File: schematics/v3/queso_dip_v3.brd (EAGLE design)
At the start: 41 x 50 mm, 43 parts, among them U1 PRTR5V0U2X, U2 PRTR5V0U2X, U3 PRTR5V0U2X, U4 PRTR5V0U2X, U5 PRTR5V0U2X

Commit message: added new version
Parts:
- removed R2: ?, rcl:R0805
- removed U$4, U$6, U$7: USB_TYPE_A_FEMALE_TH, imcom:USB_TYPE_A_FEMALE_TH
- added Q1: FOXSDLF/120-20, adafruit:SM49
- added SJ2: (no value), SparkFun-Retired:SJ_2
- added X1, X2, X3, X4: USB-A-HU, con-usb:USB-A-HU
- C1, C2, C3, C4, C5, C6: value 10uF -> VJ1210V106ZXJTW1BC
- F1, F2, F3, F4: value (none) -> PTS12066V110
- LED1, LED2, LED3, LED4, LED5: value (none) -> 150080BS75000
- R5, R6, R7: value 330R -> ERJ-6ENF3300V
- U$10: value (none) -> USB-PWR; device adafruit:CERM_OSC -> adafruit:USB-MINIB-THM-MOLEX-PWRONLY
- U$3: value USB_TYPE_A_FEMALE_TH -> MP1584EN; device imcom:USB_TYPE_A_FEMALE_TH -> power_supply:MP1584EN
- U$8: value USB-MINIB-5PIN -> 10118194-0001LF
- U1, U2, U3, U4, U5: value PRTR5V0U2X -> PRTR5V0U2X,215
- moved PAD1 46.4 mm to (26.5, 46.8)
- moved PAD2 46.4 mm to (31.5, 46.8)
- moved U$3 26.6 mm to (22.9, 27.6), turned to 90 degrees
- moved U$9 24.6 mm to (9.70, 10.0), turned to 0 degrees
- moved U$10 22.6 mm to (12.1, 3.50), turned to 0 degrees
- moved U5 14.9 mm to (10.2, 25.0)
- moved C6 12.8 mm to (18.0, 30.3), turned to 270 degrees
- moved F4 6.70 mm to (27.2, 10.1), turned to 270 degrees
- moved C5 6.38 mm to (23.7, 29.4), turned to 180 degrees
- moved C1 5.02 mm to (21.1, 10.6), flipped to the top, turned to 0 degrees
- moved LED4 4.00 mm to (14.0, 36.5)
- moved LED5 4.00 mm to (11.5, 36.5)
- moved R6 3.86 mm to (16.3, 35.9)
- moved C3 3.13 mm to (24.2, 24.4)
- moved F1 3.06 mm to (27.4, 24.4), flipped to the bottom
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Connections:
- removed net N$23: R2.1, U$1.26
- removed net N$9: F2.2, U$7.1
- new net N$1: F2.2, X1.VBUS
- new net VOUT2: SJ2.2, U$3.VOUT
- new net V_UP: U$1.18, U$8.VBUS
- net CHR_IN: now also SJ2.1
- net DM1: now also X4.D-; no longer U$3.2
- net DM2: now also X3.D-; no longer U$4.2
- net DM3: now also X2.D-; no longer U$6.2
- net DM4: now also X1.D-; no longer U$7.2
- net DP1: now also X4.D+; no longer U$3.3
- net DP2: now also X3.D+; no longer U$4.3
- net DP3: now also X2.D+; no longer U$6.3
- net DP4: now also X1.D+; no longer U$7.3
- net GND: now also U$1.27, U$10.GND, U$3.GNDIN, U$3.GNDOUT, X1.GND, X2.GND, X3.GND, X4.GND; no longer U$10.P$2, U$3.4, U$4.4, U$6.4, U$7.4
- net N$10: now also X2.VBUS; no longer U$6.1
- net N$11: now also X3.VBUS; no longer U$4.1
- net N$12: now also X4.VBUS; no longer U$3.1
- net N$27: now also Q1.2; no longer U$10.P$1
- net N$28: now also Q1.1; no longer U$10.P$3
- net VCC: now also U$1.25, U$1.26, U$10.VBUS; no longer R2.2
- net VIN: now also U$3.VIN
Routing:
- net GND: track 398.2 -> 514.5 mm, vias 10 -> 7
- net VIN: track 36.3 -> 99.7 mm
- net V_UP: track 0.00 -> 22.1 mm, vias 0 -> 1
- net VOUT: track 8.87 -> 29.0 mm
- net VCC: track 152.2 -> 165.7 mm, vias 11 -> 9
- net N$18: track 39.7 -> 30.7 mm
- net DM2: track 32.7 -> 24.1 mm
- net N$23: track 8.09 -> 0.00 mm
- net N$32: track 23.7 -> 17.8 mm
- net N$28: track 8.02 -> 13.9 mm, vias 0 -> 1
- net DP4: track 23.5 -> 18.7 mm
- net DMU: track 31.4 -> 35.8 mm, vias 1 -> 2
- net DPU: track 31.4 -> 35.7 mm, vias 1 -> 2
- net N$9: track 3.38 -> 0.00 mm
- net DM3: track 23.6 -> 26.7 mm
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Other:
- board text added: "JKW v0.2"
- board text added: "QUESO DIP"
- board text removed: "SALSA DIP"

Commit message: routing for version3
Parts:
- removed U$10: USB-PWR, adafruit:USB-MINIB-THM-MOLEX-PWRONLY
- added C7: 100nF, rcl:C0805
- moved SJ2 58.4 mm to (9.30, 44.6), flipped to the bottom, turned to 180 degrees
- moved JP1 34.3 mm to (29.9, 40.0)
- moved C4 28.2 mm to (8.30, 18.0), flipped to the top
- moved F3 28.2 mm to (16.9, 13.0), turned to 270 degrees
- moved U3 27.7 mm to (17.7, 13.0), flipped to the bottom, turned to 315 degrees
- moved U2 21.4 mm to (23.2, 12.2), flipped to the bottom, turned to 270 degrees
- moved F4 19.2 mm to (8.30, 13.3)
- moved R7 17.9 mm to (23.9, 30.5)
- moved U4 16.9 mm to (9.80, 15.0), turned to 315 degrees
- moved LED5 14.8 mm to (25.0, 30.5)
- moved R5 14.7 mm to (31.9, 30.5)
- moved LED4 14.3 mm to (27.0, 30.5)
- moved C1 14.2 mm to (33.2, 18.0), turned to 270 degrees
- moved LED3 13.9 mm to (29.0, 30.5)
- moved LED2 13.5 mm to (31.1, 30.5)
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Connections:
- net GND: now also C7.1; no longer U$10.GND
- net VCC: now also C7.2; no longer U$10.VBUS
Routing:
- net GND: track 514.5 -> 282.7 mm, vias 7 -> 12
- net VIN: track 99.7 -> 53.6 mm, vias 0 -> 4
- net N$2: track 0.00 -> 13.8 mm
- net VOUT2: track 0.00 -> 13.8 mm
- net DPU: track 35.7 -> 22.9 mm, vias 2 -> 1
- net DP2: track 29.8 -> 18.1 mm
- net DM3: track 26.7 -> 17.0 mm
- net DP3: track 26.3 -> 17.2 mm
- net DM1: track 31.8 -> 24.4 mm
- net DP1: track 31.1 -> 24.8 mm
- net DM2: track 24.1 -> 18.2 mm
- net N$24: track 9.16 -> 15.0 mm, vias 1 -> 0
- net DMU: track 35.8 -> 30.0 mm, vias 2 -> 1
- net N$25: track 6.40 -> 12.1 mm, vias 1 -> 0
- net N$27: track 11.4 -> 5.97 mm
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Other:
- board text added: "5v in"
- board text added: "7-28v"
- board text added: "JKW v0.3"
- board text removed: "JKW v0.2"

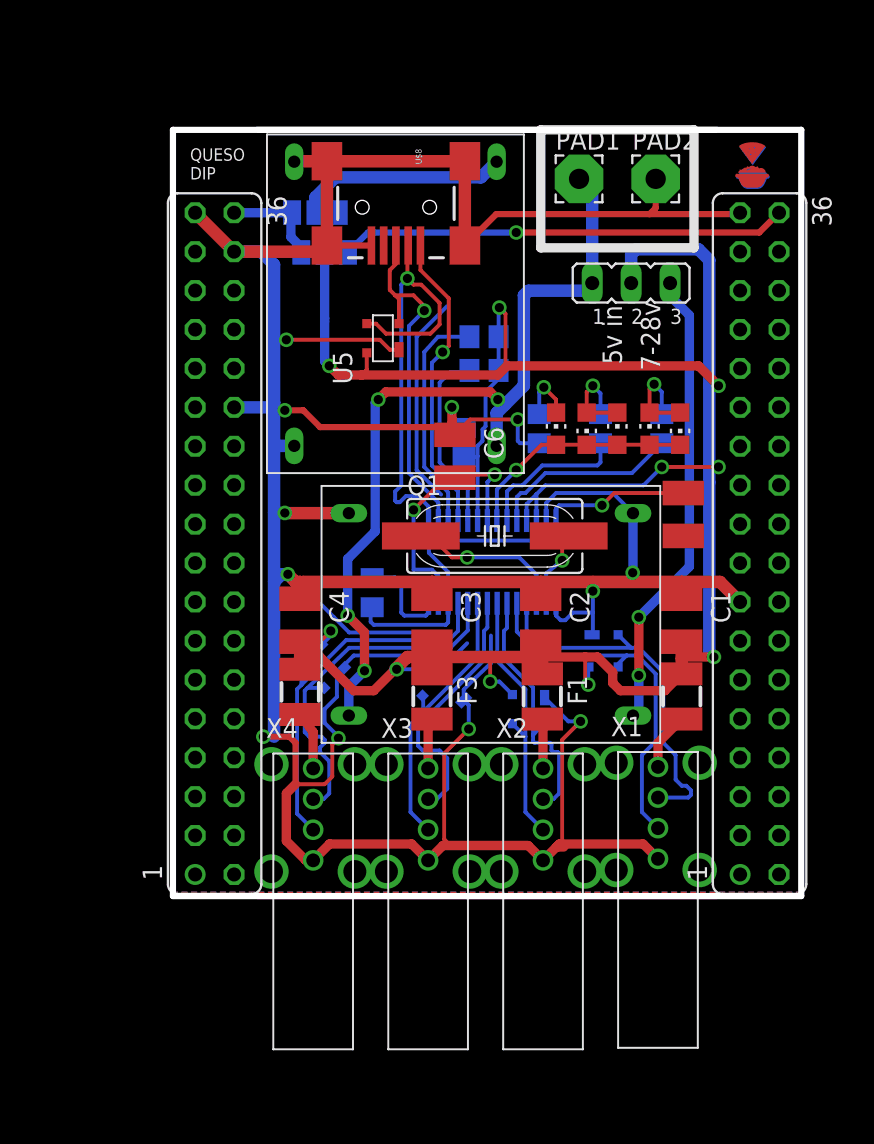
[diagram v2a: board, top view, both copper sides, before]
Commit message: improved silkscreen
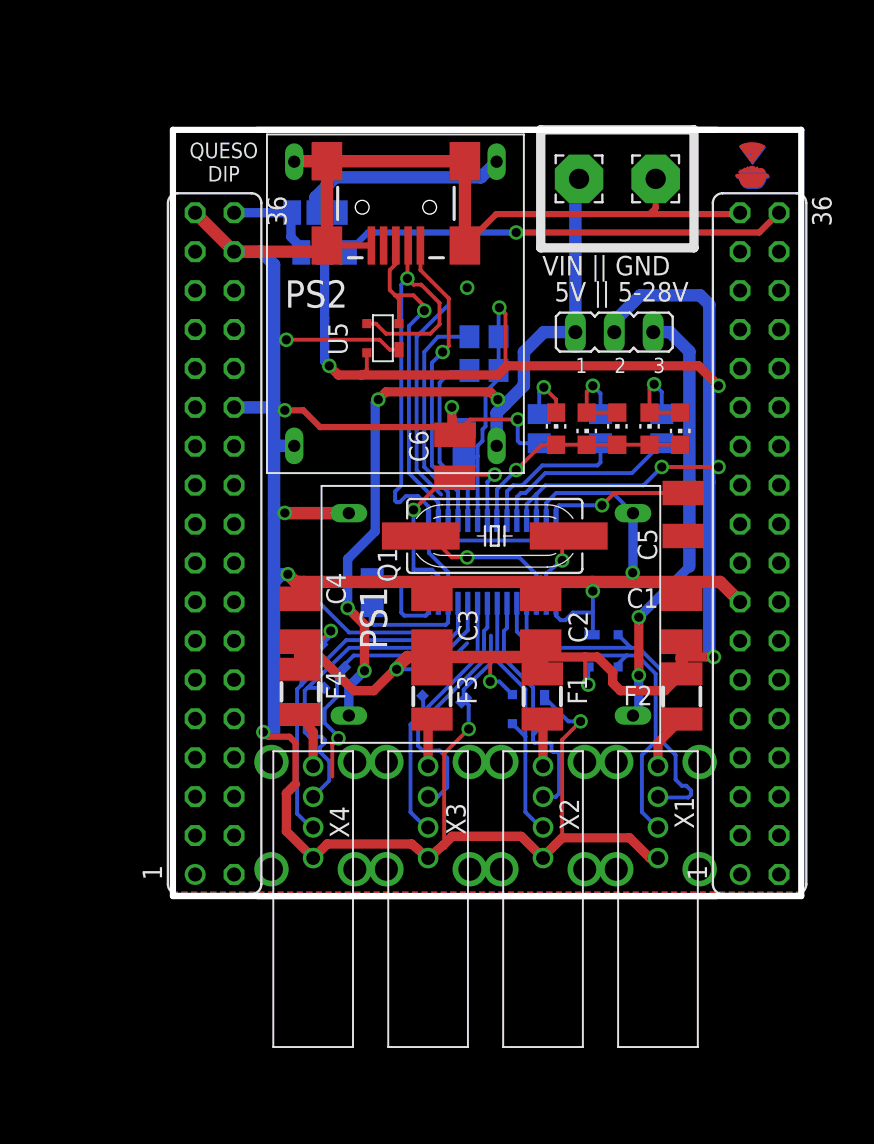
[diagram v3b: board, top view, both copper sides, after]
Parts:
- moved JP1 3.38 mm to (28.8, 36.8)
- moved X2 0.15 mm to (24.1, 1.75)
- moved X3 0.15 mm to (16.6, 1.75)
- moved X4 0.15 mm to (9.15, 1.75)
- moved X1 0.05 mm to (31.6, 1.75)
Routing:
- net N$2: track 13.8 -> 0.00 mm
- net GND: track 282.7 -> 292.2 mm, vias 12 -> 13
- net VCC: track 161.7 -> 159.2 mm
- net VOUT: track 30.3 -> 28.2 mm
- net VIN: track 53.6 -> 52.0 mm
- net DM1: track 24.4 -> 23.8 mm
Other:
- board text added: "2 PSs: (1) HUB, (2) CHIP: A 2 PSs: Combine: A&C 1 PS (assemble PS1): C 0 PS Passive Hub - Close D"
- board text added: "5V || 5-28V"
- board text added: "A"
- board text added: "C"
- board text added: "D"
- board text added: "PS1"
- board text added: "PS2"
- board text added: "VIN || GND"
- board text removed: "5v in"
- board text removed: "7-28v"
- board text removed: "JKW v3.9"

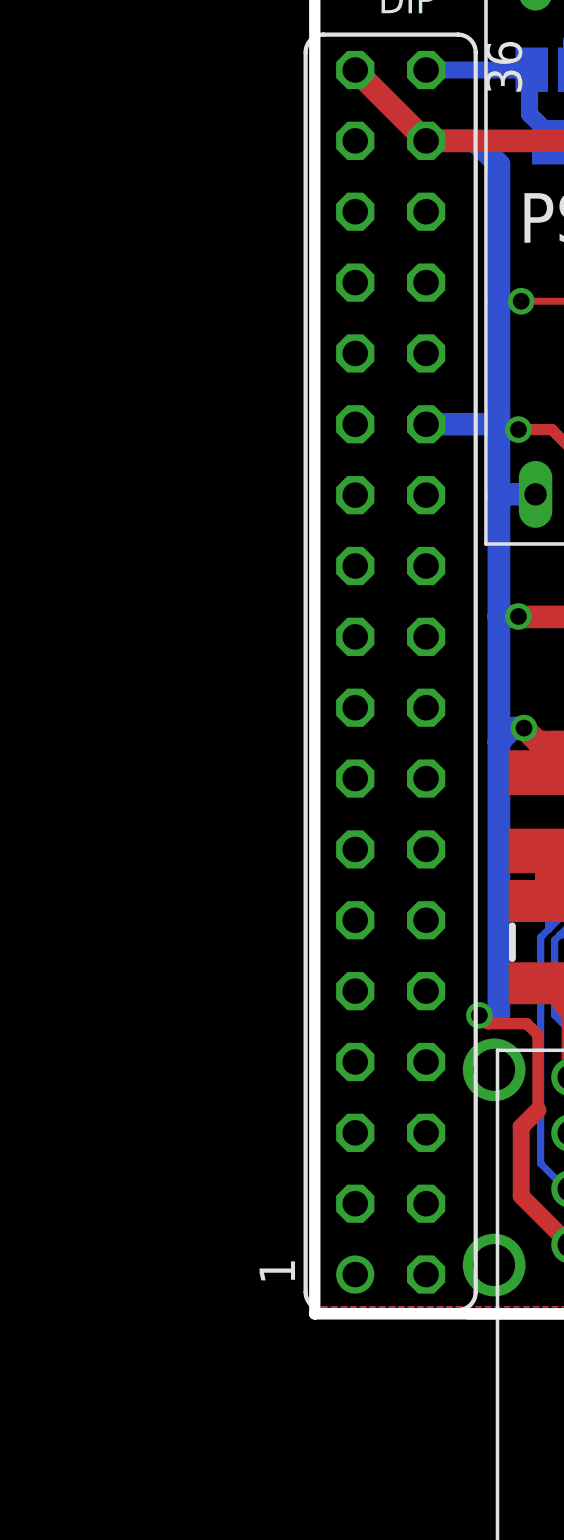
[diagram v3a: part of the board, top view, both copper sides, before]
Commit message: added order notes to all boards
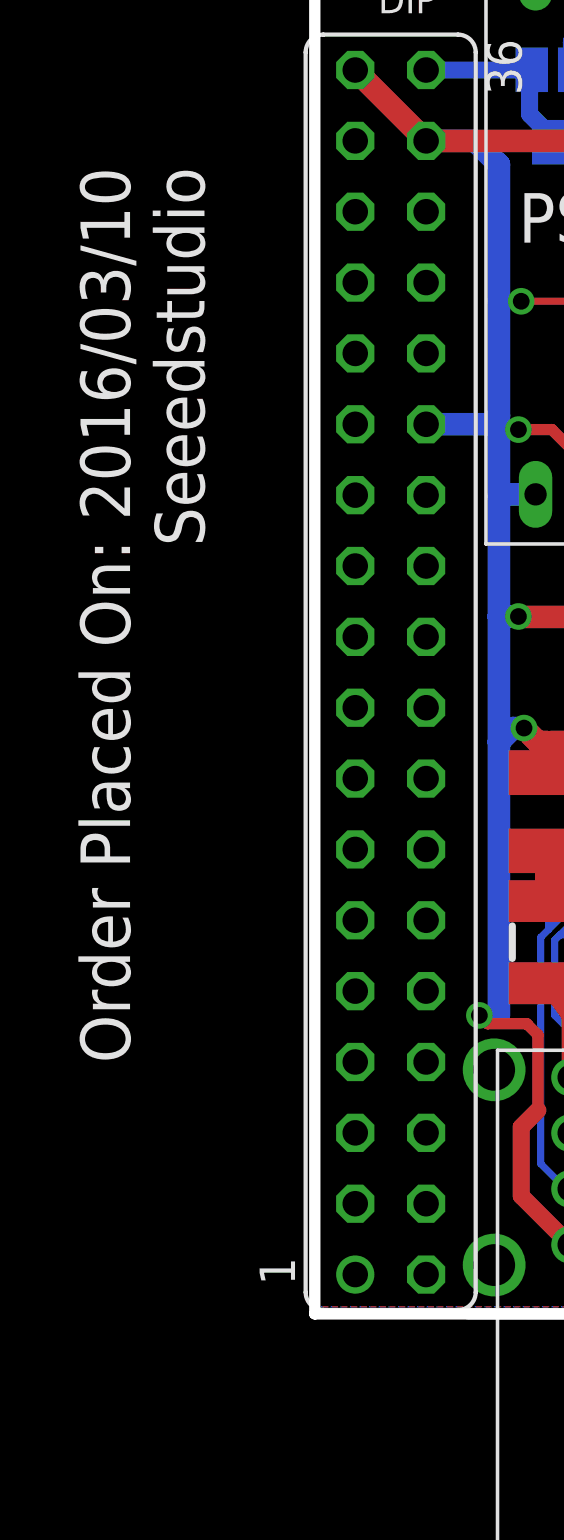
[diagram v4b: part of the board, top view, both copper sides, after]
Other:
- board text added: "Order Placed On: 2016/03/10 Seeedstudio"
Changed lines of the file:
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@@
 <circle x="39.6" y="44.6" radius="1.204159375" width="0.254" layer="26"/>
 <circle x="37" y="19.2" radius="1.204159375" width="0.254" layer="26"/>
+<text x="-8.4" y="41.1" size="1.778" layer="21" rot="R270">Order Placed On: 2016/03/10
+Seeedstudio</text>
 </plain>
 <attributes>
